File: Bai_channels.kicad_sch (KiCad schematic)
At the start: 119 parts, among them Q1 BC337, Q10 BC337, Q11 BC337, Q12 BC337, Q2 BC337, Q3 BC337, Q4 BC337, Q5 BC337, Q6 BC337, Q7 BC337, Q8 BC337, Q9 BC337, U1 ATmega328-P, U3 LM7805_TO220

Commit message: updated PCB editor
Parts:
- C1, C2, C3: footprint Custom_FP_Lib:Through-Hole Cap -> custom:capacitor
- R1, R10, R11, R12, R13, R14, R15, R16, R17, R18, R19, R2, R20, R21, R22, R23, R24, R25, R26, R27, R28, R29, R3, R30, R31, R32, R33, R5, R6, R7, R8, R9: footprint (none) -> custom:R
- R4: footprint Custom_FP_Lib:Through-Hole Resistor -> custom:R
- U4: footprint Custom_FP_Lib:Power-Source -> custom:power
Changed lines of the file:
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@@
       (effects (font (size 1.27 1.27)) (justify left))
     )
-    (property "Footprint" "Custom_FP_Lib:Through-Hole Cap" (at 46.6852 105.41 0)
+    (property "Footprint" "custom:capacitor" (at 46.6852 105.41 0)
       (effects (font (size 1.27 1.27)) hide)
     )
@@
       (effects (font (size 1.27 1.27)) hide)
     )
-    (property "Footprint" "" (at 229.87 91.948 90)
+    (property "Footprint" "custom:R" (at 229.87 91.948 90)
       (effects (font (size 1.27 1.27)) hide)
     )
@@
       (effects (font (size 1.27 1.27)) hide)
     )
-    (property "Footprint" "" (at 217.17 91.948 90)
+    (property "Footprint" "custom:R" (at 217.17 91.948 90)
       (effects (font (size 1.27 1.27)) hide)
     )
@@
       (effects (font (size 1.27 1.27)) hide)
     )
-    (property "Footprint" "" (at 179.07 119.888 90)
+    (property "Footprint" "custom:R" (at 179.07 119.888 90)
       (effects (font (size 1.27 1.27)) hide)
     )
@@
       (effects (font (size 1.27 1.27)) hide)
     )
-    (property "Footprint" "" (at 229.87 133.858 90)
+    (property "Footprint" "custom:R" (at 229.87 133.858 90)
       (effects (font (size 1.27 1.27)) hide)
     )
@@
       (effects (font (size 1.27 1.27)) hide)
     )
-    (property "Footprint" "" (at 204.47 64.008 90)
+    (property "Footprint" "custom:R" (at 204.47 64.008 90)
       (effects (font (size 1.27 1.27)) hide)
     )
@@
       (effects (font (size 1.27 1.27)))
     )
-    (property "Footprint" "Custom_FP_Lib:Power-Source" (at 15.24 93.98 0)
+    (property "Footprint" "custom:power" (at 15.24 93.98 0)
       (effects (font (size 1.27 1.27)) hide)
     )
@@
       (effects (font (size 1.27 1.27)) hide)
     )
-    (property "Footprint" "" (at 242.57 91.948 90)
+    (property "Footprint" "custom:R" (at 242.57 91.948 90)
       (effects (font (size 1.27 1.27)) hide)
     )
@@
       (effects (font (size 1.27 1.27)) hide)
     )
-    (property "Footprint" "" (at 176.53 64.008 90)
+    (property "Footprint" "custom:R" (at 176.53 64.008 90)
       (effects (font (size 1.27 1.27)) hide)
     )
@@
       (effects (font (size 1.27 1.27)) hide)
     )
-    (property "Footprint" "" (at 204.47 91.948 90)
+    (property "Footprint" "custom:R" (at 204.47 91.948 90)
       (effects (font (size 1.27 1.27)) hide)
     )
@@
       (effects (font (size 1.27 1.27)) hide)
     )
-    (property "Footprint" "" (at 191.77 119.888 90)
+    (property "Footprint" "custom:R" (at 191.77 119.888 90)
       (effects (font (size 1.27 1.27)) hide)
     )
@@
       (effects (font (size 1.27 1.27)) hide)
     )
-    (property "Footprint" "" (at 179.07 105.918 90)
+    (property "Footprint" "custom:R" (at 179.07 105.918 90)
       (effects (font (size 1.27 1.27)) hide)
     )
@@
       (effects (font (size 1.27 1.27)) hide)
     )
-    (property "Footprint" "" (at 217.17 105.918 90)
+    (property "Footprint" "custom:R" (at 217.17 105.918 90)
       (effects (font (size 1.27 1.27)) hide)
     )
@@
       (effects (font (size 1.27 1.27)) hide)
     )
-    (property "Footprint" "" (at 229.87 105.918 90)
+    (property "Footprint" "custom:R" (at 229.87 105.918 90)
       (effects (font (size 1.27 1.27)) hide)
     )
@@
       (effects (font (size 1.27 1.27)) hide)
     )
-    (property "Footprint" "" (at 242.57 119.888 90)
+    (property "Footprint" "custom:R" (at 242.57 119.888 90)
       (effects (font (size 1.27 1.27)) hide)
     )
@@
       (effects (font (size 1.27 1.27)) hide)
     )
-    (property "Footprint" "" (at 204.47 105.918 90)
+    (property "Footprint" "custom:R" (at 204.47 105.918 90)
       (effects (font (size 1.27 1.27)) hide)
     )
@@
       (effects (font (size 1.27 1.27)) hide)
     )
-    (property "Footprint" "" (at 242.57 133.858 90)
+    (property "Footprint" "custom:R" (at 242.57 133.858 90)
       (effects (font (size 1.27 1.27)) hide)
     )
@@
       (effects (font (size 1.27 1.27)))
     )
-    (property "Footprint" "Custom_FP_Lib:Through-Hole Cap" (at 101.6 136.1948 0)
+    (property "Footprint" "custom:capacitor" (at 101.6 136.1948 0)
       (effects (font (size 1.27 1.27)) hide)
     )
@@
       (effects (font (size 1.27 1.27)) hide)
     )
-    (property "Footprint" "" (at 242.57 64.008 90)
+    (property "Footprint" "custom:R" (at 242.57 64.008 90)
       (effects (font (size 1.27 1.27)) hide)
     )
@@
       (effects (font (size 1.27 1.27)) hide)
     )
-    (property "Footprint" "" (at 191.77 105.918 90)
+    (property "Footprint" "custom:R" (at 191.77 105.918 90)
       (effects (font (size 1.27 1.27)) hide)
     )
@@
       (effects (font (size 1.27 1.27)) (justify left))
     )
-    (property "Footprint" "Custom_FP_Lib:Through-Hole Cap" (at 50.4952 125.73 0)
+    (property "Footprint" "custom:capacitor" (at 50.4952 125.73 0)
       (effects (font (size 1.27 1.27)) hide)
     )
@@
       (effects (font (size 1.27 1.27)) hide)
     )
-    (property "Footprint" "" (at 204.47 119.888 90)
+    (property "Footprint" "custom:R" (at 204.47 119.888 90)
       (effects (font (size 1.27 1.27)) hide)
     )
@@
       (effects (font (size 1.27 1.27)) hide)
     )
-    (property "Footprint" "" (at 191.77 91.948 90)
+    (property "Footprint" "custom:R" (at 191.77 91.948 90)
       (effects (font (size 1.27 1.27)) hide)
     )
@@
       (effects (font (size 1.27 1.27)) hide)
     )
-    (property "Footprint" "" (at 242.57 105.918 90)
+    (property "Footprint" "custom:R" (at 242.57 105.918 90)
       (effects (font (size 1.27 1.27)) hide)
     )
@@
       (effects (font (size 1.27 1.27)) hide)
     )
-    (property "Footprint" "" (at 229.87 77.978 90)
+    (property "Footprint" "custom:R" (at 229.87 77.978 90)
       (effects (font (size 1.27 1.27)) hide)
     )
@@
       (effects (font (size 1.27 1.27)) hide)
     )
-    (property "Footprint" "" (at 179.07 91.948 90)
+    (property "Footprint" "custom:R" (at 179.07 91.948 90)
       (effects (font (size 1.27 1.27)) hide)
     )
@@
       (effects (font (size 1.27 1.27)) hide)
     )
-    (property "Footprint" "" (at 217.17 119.888 90)
+    (property "Footprint" "custom:R" (at 217.17 119.888 90)
       (effects (font (size 1.27 1.27)) hide)
     )
@@
       (effects (font (size 1.27 1.27)) hide)
     )
-    (property "Footprint" "" (at 217.17 64.008 90)
+    (property "Footprint" "custom:R" (at 217.17 64.008 90)
       (effects (font (size 1.27 1.27)) hide)
     )
@@
       (effects (font (size 1.27 1.27)) hide)
     )
-    (property "Footprint" "" (at 179.07 77.978 90)
+    (property "Footprint" "custom:R" (at 179.07 77.978 90)
       (effects (font (size 1.27 1.27)) hide)
     )
@@
       (effects (font (size 1.27 1.27)))
     )
-    (property "Footprint" "Custom_FP_Lib:Through-Hole Cap" (at 101.6 128.5748 0)
+    (property "Footprint" "custom:capacitor" (at 101.6 128.5748 0)
       (effects (font (size 1.27 1.27)) hide)
     )
@@
       (effects (font (size 1.27 1.27)) hide)
     )
-    (property "Footprint" "" (at 229.87 119.888 90)
+    (property "Footprint" "custom:R" (at 229.87 119.888 90)
       (effects (font (size 1.27 1.27)) hide)
     )
@@
       (effects (font (size 1.27 1.27)) hide)
     )
-    (property "Footprint" "" (at 204.47 77.978 90)
+    (property "Footprint" "custom:R" (at 204.47 77.978 90)
       (effects (font (size 1.27 1.27)) hide)
     )
@@
       (effects (font (size 1.27 1.27)) hide)
     )
-    (property "Footprint" "" (at 191.77 77.978 90)
+    (property "Footprint" "custom:R" (at 191.77 77.978 90)
       (effects (font (size 1.27 1.27)) hide)
     )
@@
       (effects (font (size 1.27 1.27)) hide)
     )
-    (property "Footprint" "" (at 191.77 64.008 90)
+    (property "Footprint" "custom:R" (at 191.77 64.008 90)
       (effects (font (size 1.27 1.27)) hide)
     )
@@
       (effects (font (size 1.27 1.27)))
     )
-    (property "Footprint" "Custom_FP_Lib:Through-Hole Resistor" (at 90.17 157.988 90)
+    (property "Footprint" "custom:R" (at 90.17 157.988 90)
       (effects (font (size 1.27 1.27)) hide)
     )
@@
       (effects (font (size 1.27 1.27)) hide)
     )
-    (property "Footprint" "" (at 229.87 64.008 90)
+    (property "Footprint" "custom:R" (at 229.87 64.008 90)
       (effects (font (size 1.27 1.27)) hide)
     )
@@
       (effects (font (size 1.27 1.27)) hide)
     )
-    (property "Footprint" "" (at 217.17 77.978 90)
+    (property "Footprint" "custom:R" (at 217.17 77.978 90)
       (effects (font (size 1.27 1.27)) hide)
     )
@@
       (effects (font (size 1.27 1.27)) hide)
     )
-    (property "Footprint" "" (at 242.57 77.978 90)
+    (property "Footprint" "custom:R" (at 242.57 77.978 90)
       (effects (font (size 1.27 1.27)) hide)
     )
@@
       (effects (font (size 1.27 1.27)) (justify left))
     )
-    (property "Footprint" "Custom_FP_Lib:Through-Hole Cap" (at 30.1752 128.27 0)
-      (effects (font (size 1.27 1.27)) hide)
-    )
+    (property "Footprint" "custom:capacitor" (at 30.1752 128.27 0)
+      (effects (font (size 1.27 1.27)) hide)
+    )

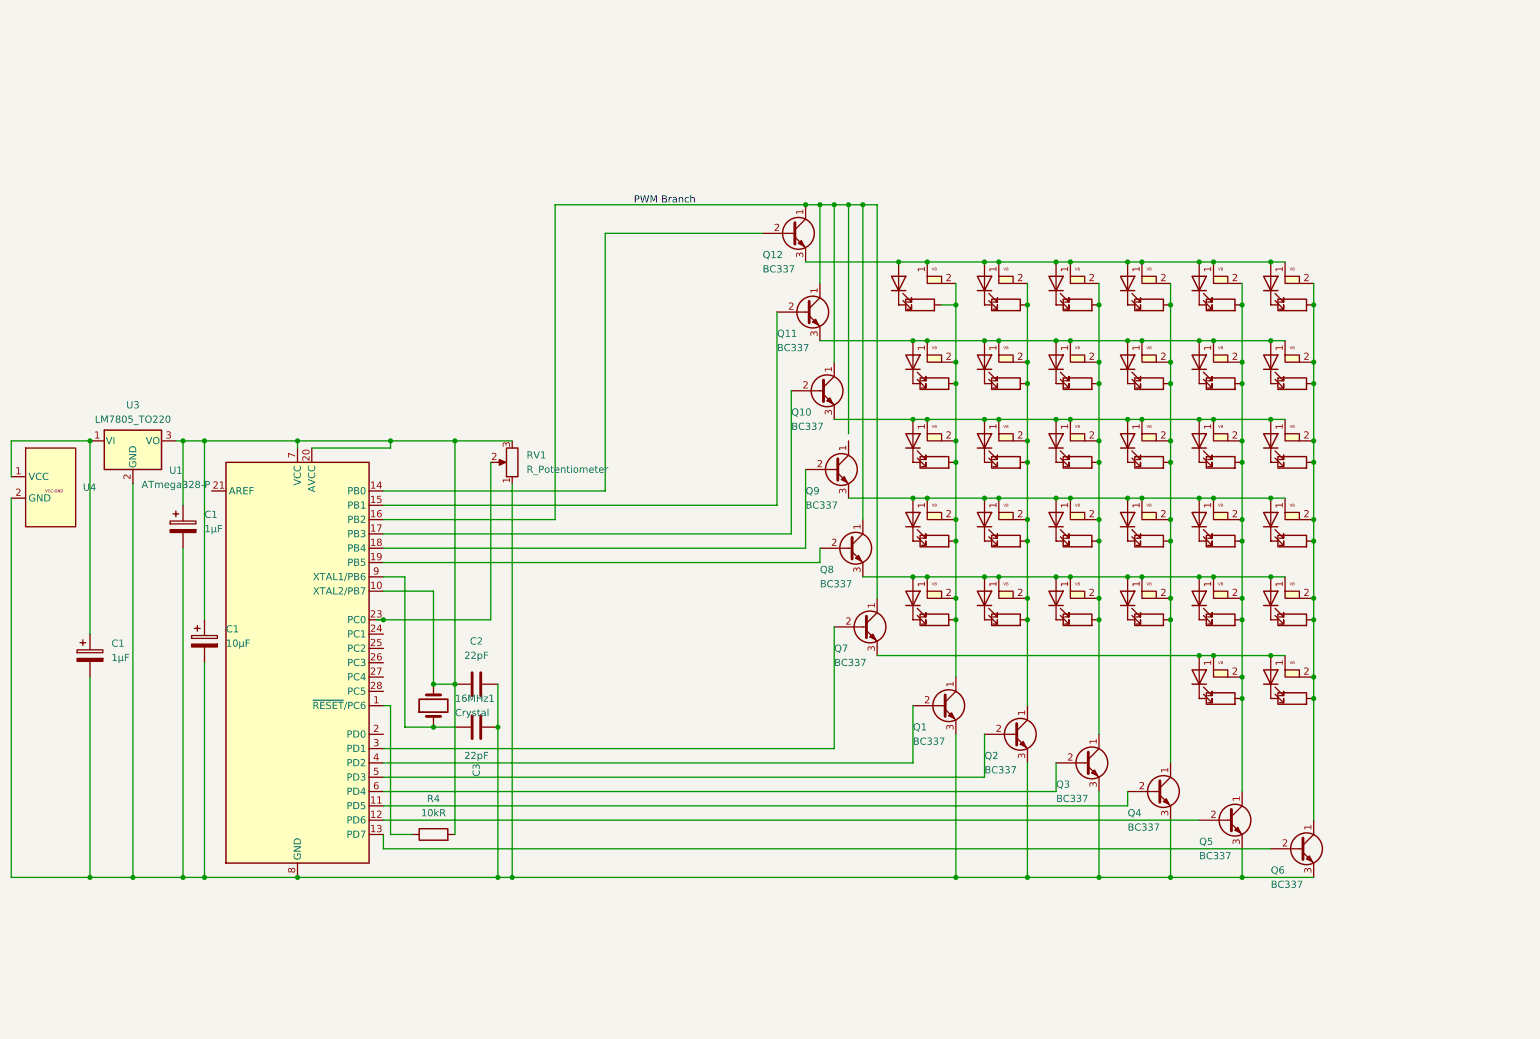
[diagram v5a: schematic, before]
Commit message: new desing to incorporate FPC Cable
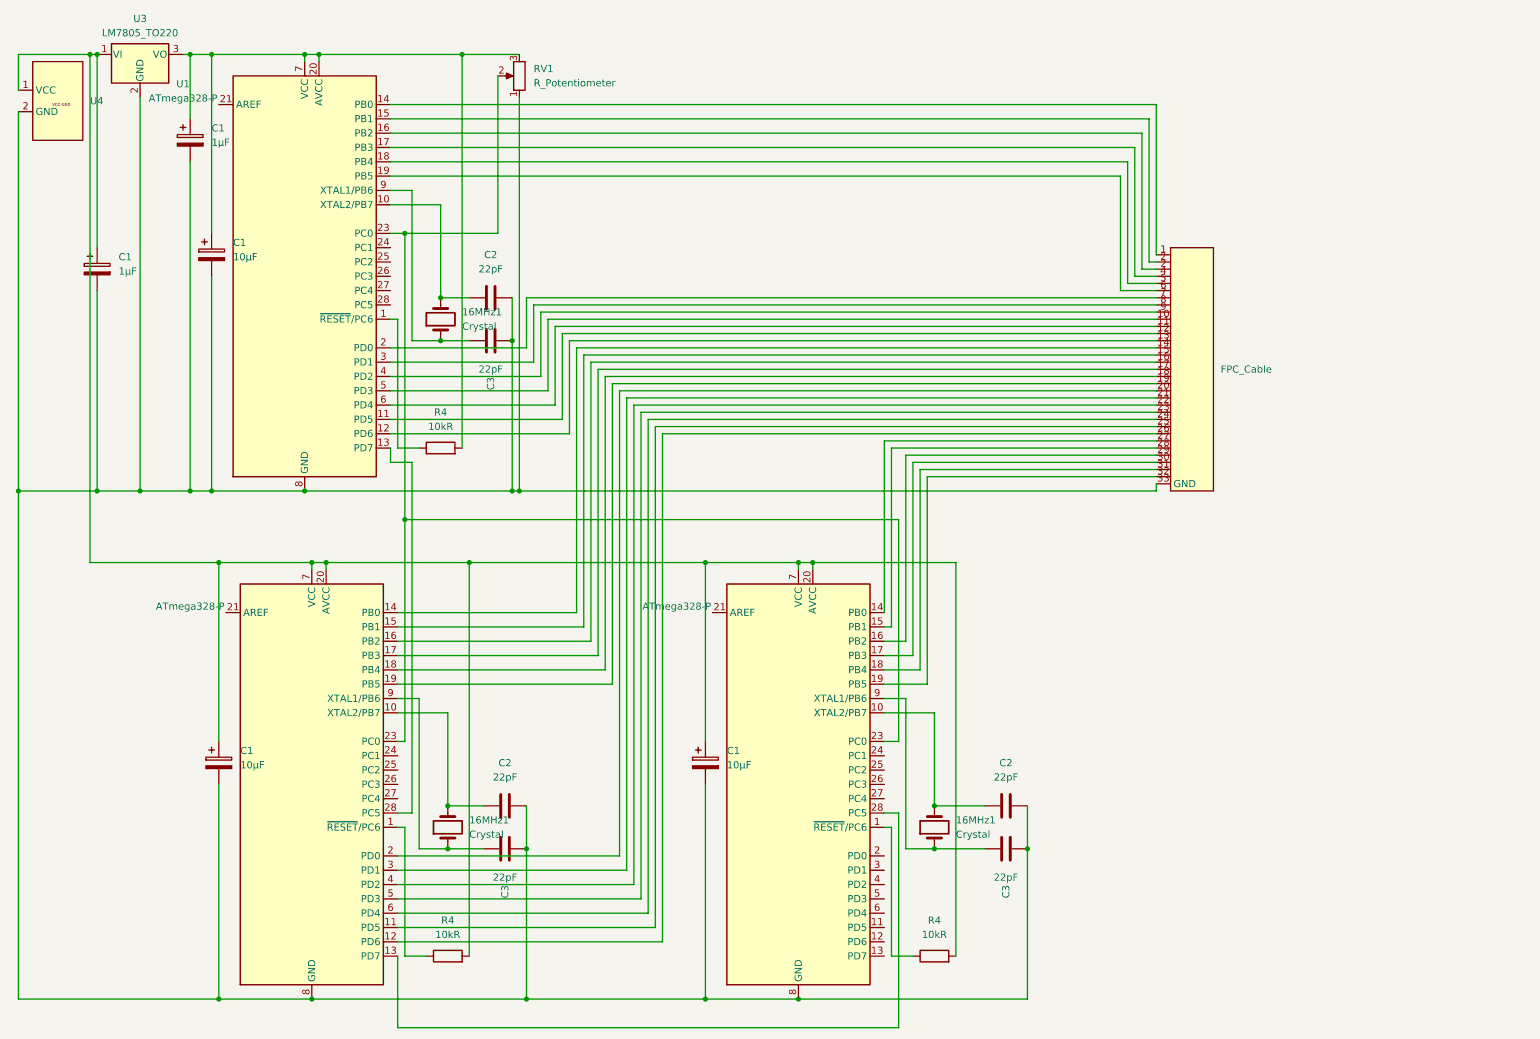
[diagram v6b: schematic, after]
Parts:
- removed D1, D10, D11, D12, D13, D14, D15, D16, D17, D18, D19, D2, D20, D21, D22, D23, D24, D25, D26, D27, D28, D29, D3, D30, D31, D32, D4, D5, D6, D7, D8, D9: LED, custom:LED, symbol Device:LED
- removed Q1, Q10, Q11, Q12, Q2, Q3, Q4, Q5, Q6, Q7, Q8, Q9: BC337, Package_TO_SOT_THT:TO-92_Inline, symbol Transistor_BJT:BC337
- removed R1, R10, R11, R12, R13, R14, R15, R16, R17, R18, R19, R2, R20, R21, R22, R23, R24, R25, R26, R27, R28, R29, R3, R30, R31, R32, R33, R5, R6, R7, R8, R9: R, custom:R, symbol Device:R
- removed U10, U11, U12, U13, U14, U16, U17, U18, U19, U20, U22, U23, U24, U25, U26, U28, U29, U30, U31, U32, U33, U34, U35, U36, U37, U38, U39, U4, U5, U6, U7, U8: ~, custom:vibration_motor, symbol Custom_Symbol_Lib:VB
- added 16MHz1 (x2): Crystal, Crystal:Crystal_HC49-4H_Vertical, symbol Device:Crystal
- added C1 (x2): 10µF, custom:capacitor, symbol Device:C_Polarized
- added C2 (x2), C3 (x2): 22pF, custom:capacitor, symbol Device:C
- added FPC_Cable: ~, symbol Custom_Symbol_Lib:FCP_Cable
- added R4 (x2): 10kR, custom:R, symbol Device:R
- added U1 (x2): ATmega328-P, Package_DIP:DIP-28_W7.62mm_Socket, symbol MCU_Microchip_ATmega:ATmega328-P
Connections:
- net at C1.1, C1.1, R4.2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: no longer 16MHz1.2, C2.1, U1.10 (XTAL2/PB7)
- net at C1.2, C1.2, C1.2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: now also C1.2, C1.2, C2.2, C2.2, C3.2, C3.2, FPC_Cable.33 (GND), U1.22 (GND), U1.22 (GND), U1.8 (GND), U1.8 (GND)
- net at U1.12 (PD6): now also FPC_Cable.13
- net at C1.1, U3.1 (VI), U4.1 (VCC): now also C1.1, C1.1, R4.2, R4.2, U1.20 (AVCC), U1.20 (AVCC), U1.7 (VCC), U1.7 (VCC)
- net at U1.5 (PD3): now also FPC_Cable.10
- net at U1.16 (PB2): now also FPC_Cable.2
- net at U1.17 (PB3): now also FPC_Cable.4
- net at U1.4 (PD2): now also FPC_Cable.9
- net at U1.11 (PD5): now also FPC_Cable.12
- net at U1.13 (PD7): now also U1.28 (PC5)
- net at U1.14 (PB0): now also FPC_Cable.1
- net at U1.15 (PB1): now also FPC_Cable.2
- net at U1.18 (PB4): now also FPC_Cable.5
- net at U1.19 (PB5): now also FPC_Cable.6
- net at U1.2 (PD0): now also FPC_Cable.7
- net at RV1.2, U1.23 (PC0): now also U1.23 (PC0), U1.23 (PC0)
- net at U1.3 (PD1): now also FPC_Cable.8
- net at U1.6 (PD4): now also FPC_Cable.11
- new net: R4.1, U1.1 (~{RESET}/PC6) (x2)
- new net: 16MHz1.1, C3.1, U1.9 (XTAL1/PB6) (x2)
- new net: FPC_Cable.14, U1.14 (PB0)
- new net: FPC_Cable.15, U1.15 (PB1)
- new net: FPC_Cable.16, U1.16 (PB2)
- new net: FPC_Cable.17, U1.17 (PB3)
- new net: FPC_Cable.18, U1.18 (PB4)
- new net: FPC_Cable.19, U1.19 (PB5)
- new net: FPC_Cable.20, U1.2 (PD0)
- new net: FPC_Cable.21, U1.3 (PD1)
- new net: FPC_Cable.22, U1.4 (PD2)
- new net: FPC_Cable.23, U1.5 (PD3)
- new net: FPC_Cable.24, U1.6 (PD4)
- new net: FPC_Cable.25, U1.11 (PD5)
- new net: FPC_Cable.26, U1.12 (PD6)
- new net: FPC_Cable.27, U1.14 (PB0)
- new net: FPC_Cable.28, U1.15 (PB1)
- new net: FPC_Cable.29, U1.16 (PB2)
- new net: FPC_Cable.30, U1.17 (PB3)
- new net: FPC_Cable.31, U1.18 (PB4)
- new net: FPC_Cable.32, U1.19 (PB5)
- new net: 16MHz1.2, C2.1, U1.10 (XTAL2/PB7) (x3)
- new net: U1.13 (PD7), U1.28 (PC5)
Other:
- note removed: "PWM Branch"
- moved on the sheet: 16MHz1, C1, C2, C3, R4, RV1, U1, U3, U4
